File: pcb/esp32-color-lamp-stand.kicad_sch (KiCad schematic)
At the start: 56 parts, among them J1 USB_C_Receptacle, U1 MIC5219-3.3YM5, U2 ESP32-WROOM-32, U3 CH340G, U4 74HCT245

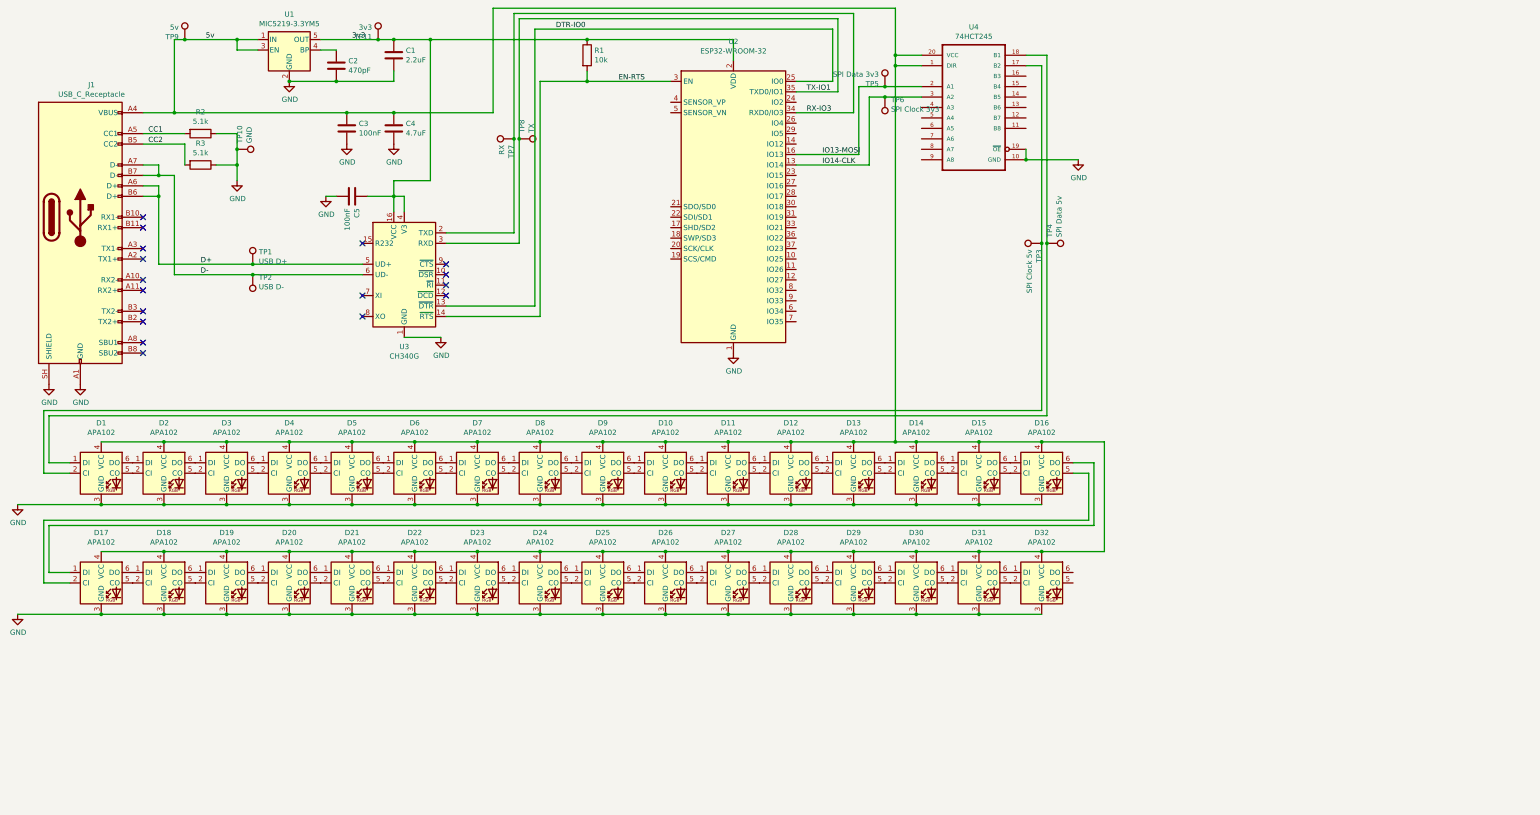
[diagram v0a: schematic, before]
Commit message: Complete ESP32-S3 PCB redesign and routing
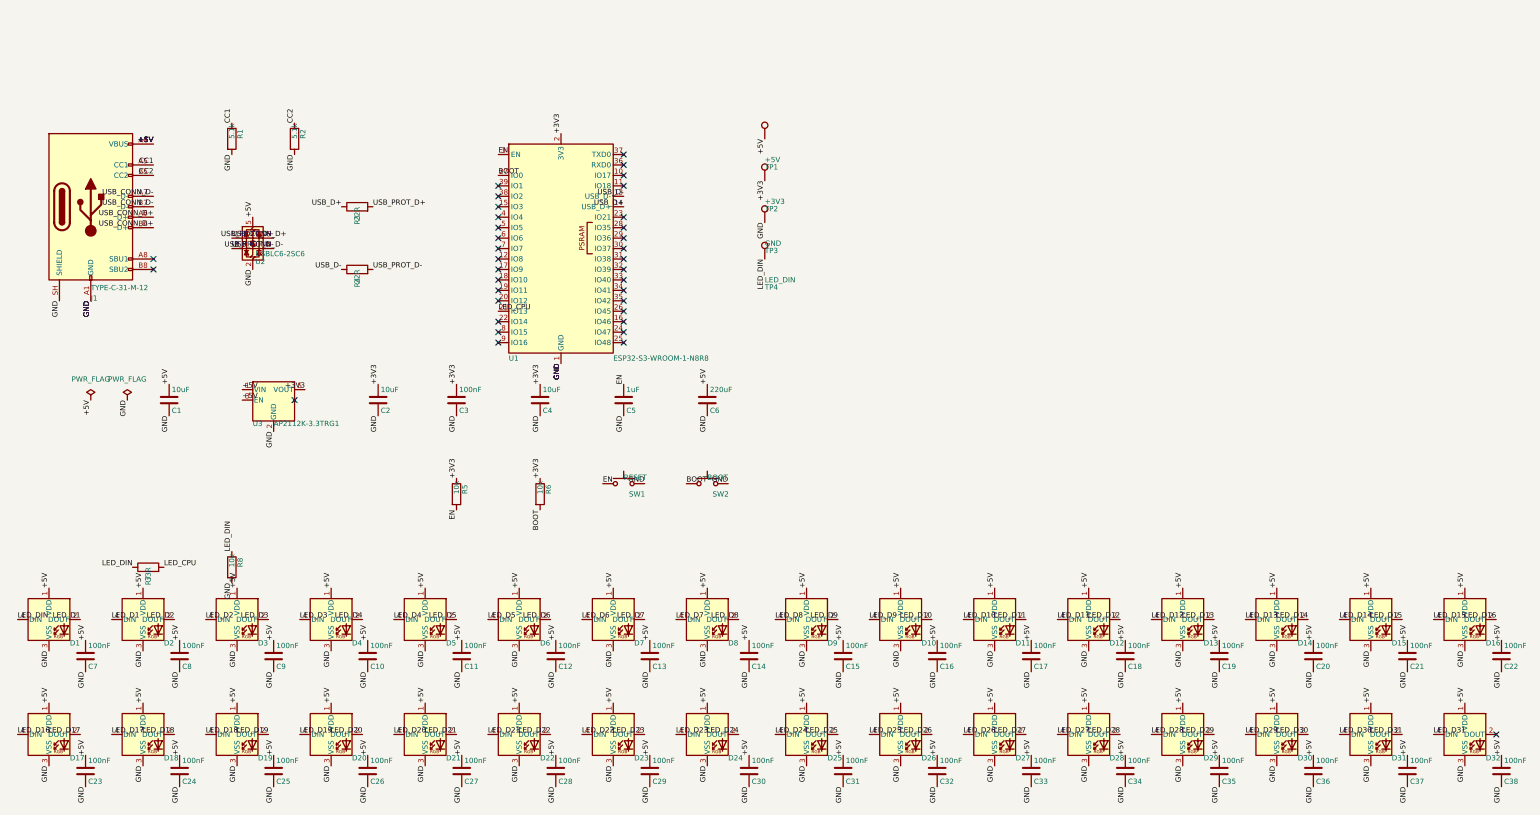
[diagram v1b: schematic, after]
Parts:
- removed D1, D10, D11, D12, D13, D14, D15, D16, D17, D18, D19, D2, D20, D21, D22, D23, D24, D25, D26, D27, D28, D29, D3, D30, D31, D32, D4, D5, D6, D7, D8, D9: APA102, LED_SMD:LED_RGB_5050-6, symbol LED:APA102
- removed J1: USB_C_Receptacle, Connector_USB:USB_C_Receptacle_Amphenol_12401610E4-2A_CircularHoles, symbol Connector:USB_C_Receptacle
- removed TP10: GND, TestPoint:TestPoint_Pad_D1.0mm, symbol Connector:TestPoint
- removed TP11: 3v3, TestPoint:TestPoint_Pad_D1.0mm, symbol Connector:TestPoint
- removed TP5: SPI Data 3v3, TestPoint:TestPoint_Pad_D1.0mm, symbol Connector:TestPoint
- removed TP6: SPI Clock 3v3, TestPoint:TestPoint_Pad_D1.0mm, symbol Connector:TestPoint
- removed TP7: RX, TestPoint:TestPoint_Pad_D1.0mm, symbol Connector:TestPoint
- removed TP8: TX, TestPoint:TestPoint_Pad_D1.0mm, symbol Connector:TestPoint
- removed TP9: 5v, TestPoint:TestPoint_Pad_D1.0mm, symbol Connector:TestPoint
- removed U1: MIC5219-3.3YM5, Package_TO_SOT_SMD:SOT-23-5, symbol Regulator_Linear:MIC5219-3.3YM5
- removed U2: ESP32-WROOM-32, RF_Module:ESP32-WROOM-32, symbol RF_Module:ESP32-WROOM-32
- removed U3: CH340G, Package_SO:SOIC-16_3.9x9.9mm_P1.27mm, symbol Interface_USB:CH340G
- removed U4: 74HCT245, 74HCT245:SSOP20, symbol 74HCT245:74HCT245
- added C10, C11, C12, C13, C14, C15, C16, C17, C18, C19, C20, C21, C22, C23, C24, C25, C26, C27, C28, C29, C30, C31, C32, C33, C34, C35, C36, C37, C38, C7, C8, C9: 100nF, Capacitor_SMD:C_0603_1608Metric, symbol Device:C
- added C6: 220uF, Capacitor_SMD:C_Elec_5x5.8, symbol Device:C
- added D1, D10, D11, D12, D13, D14, D15, D16, D17, D18, D19, D2, D20, D21, D22, D23, D24, D25, D26, D27, D28, D29, D3, D30, D31, D32, D4, D5, D6, D7, D8, D9: XL-5050RGBC-2812B-S, LED_SMD:LED_WS2812B_PLCC4_5.0x5.0mm_P3.2mm, symbol LED:WS2812B
- added J1: TYPE-C-31-M-12, Connector_USB:USB_C_Receptacle_HRO_TYPE-C-31-M-12, symbol Connector:USB_C_Receptacle_USB2.0_16P
- added R4: 22R, Resistor_SMD:R_0603_1608Metric, symbol Device:R
- added R5, R6, R8: 10k, Resistor_SMD:R_0603_1608Metric, symbol Device:R
- added R7: 33R, Resistor_SMD:R_0603_1608Metric, symbol Device:R
- added SW1: RESET, Button_Switch_SMD:SW_Push_1P1T_XKB_TS-1187A, symbol Switch:SW_Push
- added SW2: BOOT, Button_Switch_SMD:SW_Push_1P1T_XKB_TS-1187A, symbol Switch:SW_Push
- added U1: ESP32-S3-WROOM-1-N8R8, RF_Module:ESP32-S3-WROOM-1, symbol RF_Module:ESP32-S3-WROOM-1
- added U2: USBLC6-2SC6, Package_TO_SOT_SMD:SOT-23-6, symbol Power_Protection:USBLC6-2SC6
- added U3: AP2112K-3.3TRG1, Package_TO_SOT_SMD:SOT-23-5, symbol Regulator_Linear:AP2112K-3.3
- C1: value 2.2uF -> 10uF; LCSC (none) -> C15850; Manufacturer (none) -> Samsung Electro-Mechanics; Manufacturer Part Number (none) -> 10uF
- C2: value 470pF -> 10uF; LCSC (none) -> C15850; Manufacturer (none) -> Samsung Electro-Mechanics; Manufacturer Part Number (none) -> 10uF
- C3: footprint Capacitor_SMD:C_0805_2012Metric -> Capacitor_SMD:C_0603_1608Metric; LCSC (none) -> C14663; Manufacturer (none) -> Samsung Electro-Mechanics; Manufacturer Part Number (none) -> 100nF
- C4: value 4.7uF -> 10uF; LCSC (none) -> C15850; Manufacturer (none) -> Samsung Electro-Mechanics; Manufacturer Part Number (none) -> 10uF
- C5: value 100nF -> 1uF; footprint Capacitor_SMD:C_0805_2012Metric -> Capacitor_SMD:C_0603_1608Metric; LCSC (none) -> C15849; Manufacturer (none) -> Samsung Electro-Mechanics; Manufacturer Part Number (none) -> 1uF
- R1: value 10k -> 5.1k; footprint Resistor_SMD:R_0805_2012Metric -> Resistor_SMD:R_0603_1608Metric; LCSC (none) -> C23186; Manufacturer (none) -> UNI-ROYAL; Manufacturer Part Number (none) -> 5.1k
- R2: footprint Resistor_SMD:R_0805_2012Metric -> Resistor_SMD:R_0603_1608Metric; LCSC (none) -> C23186; Manufacturer (none) -> UNI-ROYAL; Manufacturer Part Number (none) -> 5.1k
- R3: value 5.1k -> 22R; footprint Resistor_SMD:R_0805_2012Metric -> Resistor_SMD:R_0603_1608Metric; LCSC (none) -> C23345; Manufacturer (none) -> UNI-ROYAL; Manufacturer Part Number (none) -> 22R
- TP1: value USB D+ -> +5V; footprint TestPoint:TestPoint_Pad_D1.0mm -> TestPoint:TestPoint_Pad_D1.5mm; LCSC (none) -> DNP; Manufacturer (none) -> DNP; Manufacturer Part Number (none) -> DNP; now left out of the parts list
- TP2: value USB D- -> +3V3; footprint TestPoint:TestPoint_Pad_D1.0mm -> TestPoint:TestPoint_Pad_D1.5mm; LCSC (none) -> DNP; Manufacturer (none) -> DNP; Manufacturer Part Number (none) -> DNP; now left out of the parts list
- TP3: value SPI Clock 5v -> GND; footprint TestPoint:TestPoint_Pad_D1.0mm -> TestPoint:TestPoint_Pad_D1.5mm; LCSC (none) -> DNP; Manufacturer (none) -> DNP; Manufacturer Part Number (none) -> DNP; now left out of the parts list
- TP4: value SPI Data 5v -> LED_DIN; footprint TestPoint:TestPoint_Pad_D1.0mm -> TestPoint:TestPoint_Pad_D1.5mm; LCSC (none) -> DNP; Manufacturer (none) -> DNP; Manufacturer Part Number (none) -> DNP; now left out of the parts list
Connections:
- net 5v is gone; now on net +3V3: C3.1, C4.1
- net D- is gone; now on net +3V3: TP2.1
- net EN-RTS is gone; now on net GND: R1.2
- net CC1: now also R1.1, J1.A5 (CC1); no longer R2.2
- net CC2: now also R2.1, J1.B5 (CC2); no longer R3.2
- net GND: now also R2.2, TP3.1, C10.2, C11.2, C12.2, C13.2, C14.2, C15.2, C16.2, C17.2, C18.2, C19.2, C20.2, C21.2, C22.2, C23.2, C24.2, C25.2, C26.2, C27.2, C28.2, C29.2, C30.2, C31.2, C32.2, C33.2, C34.2, C35.2, C36.2, C37.2, C38.2, C6.2, C7.2, C8.2, C9.2, D1.3 (VSS), D10.3 (VSS), D11.3 (VSS), D12.3 (VSS), D13.3 (VSS), D14.3 (VSS), D15.3 (VSS), D16.3 (VSS), D17.3 (VSS), D18.3 (VSS), D19.3 (VSS), D2.3 (VSS), D20.3 (VSS), D21.3 (VSS), D22.3 (VSS), D23.3 (VSS), D24.3 (VSS), D25.3 (VSS), D26.3 (VSS), D27.3 (VSS), D28.3 (VSS), D29.3 (VSS), D3.3 (VSS), D30.3 (VSS), D31.3 (VSS), D32.3 (VSS), D4.3 (VSS), D5.3 (VSS), D6.3 (VSS), D7.3 (VSS), D8.3 (VSS), D9.3 (VSS), J1.A1 (GND), J1.A12 (GND), J1.B1 (GND), J1.B12 (GND), J1.SH (SHIELD), R8.2, SW1.2, SW2.2, U1.1 (GND), U1.40 (GND), U1.41 (GND), U2.2 (GND), U3.2 (GND); no longer R2.1, R3.1
- net +3V3: now reaches C2.1
- net +3V3: now also R5.1, R6.1, U1.2 (3V3), U3.5 (VOUT)
- net LED_DIN: now reaches TP4.1
- net LED_DIN: now also D1.4 (DIN), R7.1, R8.1
- removed net 3v3: C1.1, C5.1, R1.1
- net D+ renamed +5V
- net +5V: now also C1.1, C10.1, C11.1, C12.1, C13.1, C14.1, C15.1, C16.1, C17.1, C18.1, C19.1, C20.1, C21.1, C22.1, C23.1, C24.1, C25.1, C26.1, C27.1, C28.1, C29.1, C30.1, C31.1, C32.1, C33.1, C34.1, C35.1, C36.1, C37.1, C38.1, C6.1, C7.1, C8.1, C9.1, D1.1 (VDD), D10.1 (VDD), D11.1 (VDD), D12.1 (VDD), D13.1 (VDD), D14.1 (VDD), D15.1 (VDD), D16.1 (VDD), D17.1 (VDD), D18.1 (VDD), D19.1 (VDD), D2.1 (VDD), D20.1 (VDD), D21.1 (VDD), D22.1 (VDD), D23.1 (VDD), D24.1 (VDD), D25.1 (VDD), D26.1 (VDD), D27.1 (VDD), D28.1 (VDD), D29.1 (VDD), D3.1 (VDD), D30.1 (VDD), D31.1 (VDD), D32.1 (VDD), D4.1 (VDD), D5.1 (VDD), D6.1 (VDD), D7.1 (VDD), D8.1 (VDD), D9.1 (VDD), J1.A4 (VBUS), J1.A9 (VBUS), J1.B4 (VBUS), J1.B9 (VBUS), U2.5 (VBUS), U3.1 (VIN), U3.3 (EN)
- new net BOOT: R6.2, SW2.1, U1.27 (IO0)
- new net EN: C5.1, R5.2, SW1.1, U1.3 (EN)
- new net LED_CPU: R7.2, U1.21 (IO13)
- new net LED_D1: D1.2 (DOUT), D2.4 (DIN)
- new net LED_D10: D10.2 (DOUT), D11.4 (DIN)
- new net LED_D11: D11.2 (DOUT), D12.4 (DIN)
- new net LED_D12: D12.2 (DOUT), D13.4 (DIN)
- new net LED_D13: D13.2 (DOUT), D14.4 (DIN)
- new net LED_D14: D14.2 (DOUT), D15.4 (DIN)
- new net LED_D15: D15.2 (DOUT), D16.4 (DIN)
- new net LED_D16: D16.2 (DOUT), D17.4 (DIN)
- new net LED_D17: D17.2 (DOUT), D18.4 (DIN)
- new net LED_D18: D18.2 (DOUT), D19.4 (DIN)
- new net LED_D19: D19.2 (DOUT), D20.4 (DIN)
- new net LED_D2: D2.2 (DOUT), D3.4 (DIN)
- new net LED_D20: D20.2 (DOUT), D21.4 (DIN)
- new net LED_D21: D21.2 (DOUT), D22.4 (DIN)
- new net LED_D22: D22.2 (DOUT), D23.4 (DIN)
- new net LED_D23: D23.2 (DOUT), D24.4 (DIN)
- new net LED_D24: D24.2 (DOUT), D25.4 (DIN)
- new net LED_D25: D25.2 (DOUT), D26.4 (DIN)
- new net LED_D26: D26.2 (DOUT), D27.4 (DIN)
- new net LED_D27: D27.2 (DOUT), D28.4 (DIN)
- new net LED_D28: D28.2 (DOUT), D29.4 (DIN)
- new net LED_D29: D29.2 (DOUT), D30.4 (DIN)
- new net LED_D3: D3.2 (DOUT), D4.4 (DIN)
- new net LED_D30: D30.2 (DOUT), D31.4 (DIN)
- new net LED_D31: D31.2 (DOUT), D32.4 (DIN)
- new net LED_D4: D4.2 (DOUT), D5.4 (DIN)
- new net LED_D5: D5.2 (DOUT), D6.4 (DIN)
- new net LED_D6: D6.2 (DOUT), D7.4 (DIN)
- new net LED_D7: D7.2 (DOUT), D8.4 (DIN)
- new net LED_D8: D8.2 (DOUT), D9.4 (DIN)
- new net LED_D9: D10.4 (DIN), D9.2 (DOUT)
- new net USB_CONN_D+: J1.A6 (D+), J1.B6 (D+), U2.1 (I/O1)
- new net USB_CONN_D-: J1.A7 (D-), J1.B7 (D-), U2.3 (I/O2)
- new net USB_D+: R3.1, U1.14 (USB_D+)
- new net USB_D-: R4.1, U1.13 (USB_D-)
- new net USB_PROT_D+: R3.2, U2.6 (I/O1)
- new net USB_PROT_D-: R4.2, U2.4 (I/O2)
- no-connect marks 17 -> 36
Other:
- title: (none) -> esp32-color-lamp-stand

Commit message: Finalize ESP32-S3 PCB and manufacturing workflow
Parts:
- removed C6: 220uF, Capacitor_SMD:C_Elec_5x5.8, symbol Device:C
- added C39, C42, C43: 100nF, Capacitor_SMD:C_0603_1608Metric, symbol Device:C
- added C40: 10nF, Capacitor_SMD:C_0603_1608Metric, symbol Device:C
- added C41: 1uF, Capacitor_SMD:C_0603_1608Metric, symbol Device:C
- added C6: 220uF, Capacitor_SMD:C_Elec_6.3x5.8, symbol Device:C_Polarized
- added R10, R11, R12, R9: 100k, Resistor_SMD:R_0603_1608Metric, symbol Device:R
- added TP5: LED_5V, TestPoint:TestPoint_Pad_D1.0mm, symbol Connector:TestPoint
- added U4: 74AHCT1G125W5-7, Package_TO_SOT_SMD:SOT-23-5, symbol 74xGxx:74AHCT1G125
- added U5: TPS22975DSGR, Package_SON:Texas_DSG0008A_WSON-8-1EP_2x2mm_P0.5mm_EP0.9x1.6mm, symbol esp32-color-lamp-stand-symbols:TPS22975DSGR
- C1: value 10uF -> 4.7uF; LCSC C15850 -> C1779; Manufacturer Part Number 10uF -> 4.7uF
- R7: value 33R -> 470R; LCSC C23140 -> C23179; Manufacturer Part Number 33R -> 470R
- TP1, TP2, TP3, TP4: footprint TestPoint:TestPoint_Pad_D1.5mm -> TestPoint:TestPoint_Pad_D1.0mm
- U3: LCSC C51118 -> C23380830
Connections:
- net +3V3: now also U5.3 (ON)
- net +5V: now also C41.1, U5.4 (VIN), U5.5 (VBIAS), U5.6 (VIN); no longer C10.1, C11.1, C12.1, C13.1, C14.1, C15.1, C16.1, C17.1, C18.1, C19.1, C20.1, C21.1, C22.1, C23.1, C24.1, C25.1, C26.1, C27.1, C28.1, C29.1, C30.1, C31.1, C32.1, C33.1, C34.1, C35.1, C36.1, C37.1, C38.1, C7.1, C8.1, C9.1, D1.1 (VDD), D10.1 (VDD), D11.1 (VDD), D12.1 (VDD), D13.1 (VDD), D14.1 (VDD), D15.1 (VDD), D16.1 (VDD), D17.1 (VDD), D18.1 (VDD), D19.1 (VDD), D2.1 (VDD), D20.1 (VDD), D21.1 (VDD), D22.1 (VDD), D23.1 (VDD), D24.1 (VDD), D25.1 (VDD), D26.1 (VDD), D27.1 (VDD), D28.1 (VDD), D29.1 (VDD), D3.1 (VDD), D30.1 (VDD), D31.1 (VDD), D32.1 (VDD), D4.1 (VDD), D5.1 (VDD), D6.1 (VDD), D7.1 (VDD), D8.1 (VDD), D9.1 (VDD)
- net BOOT: now also SW2.2; no longer SW2.1
- net CC1: now also R9.1
- net CC2: now also R10.1
- net EN: now also SW1.2; no longer SW1.1
- net GND: now also SW1.1, SW2.1, C39.2, C40.2, C41.2, C42.2, C43.2, C6.2, R11.2, R12.2, U4.1, U4.3 (GND), U5.2 (GND), U5.9 (EP); no longer SW1.2, SW2.2
- net LED_CPU: now also R8.1, U4.2; no longer R7.2
- net LED_DIN: no longer R8.1
- net CC1_ADC: now reaches U1.4 (IO4)
- net CC1_ADC: now also C42.1, R11.1, R9.2
- net CC2_ADC: now reaches U1.5 (IO5)
- net CC2_ADC: now also C43.1, R10.2, R12.1
- net LED_D1: no longer names the net of D1.2 (DOUT), D2.4 (DIN)
- net LED_D10: no longer names the net of D10.2 (DOUT), D11.4 (DIN)
- net LED_D11: no longer names the net of D11.2 (DOUT), D12.4 (DIN)
- net LED_D12: no longer names the net of D12.2 (DOUT), D13.4 (DIN)
- net LED_D13: no longer names the net of D13.2 (DOUT), D14.4 (DIN)
- net LED_D14: no longer names the net of D14.2 (DOUT), D15.4 (DIN)
- net LED_D15: no longer names the net of D15.2 (DOUT), D16.4 (DIN)
- net LED_D17: no longer names the net of D17.2 (DOUT), D18.4 (DIN)
- net LED_D18: no longer names the net of D18.2 (DOUT), D19.4 (DIN)
- net LED_D19: no longer names the net of D19.2 (DOUT), D20.4 (DIN)
- net LED_D2: no longer names the net of D2.2 (DOUT), D3.4 (DIN)
- net LED_D20: no longer names the net of D20.2 (DOUT), D21.4 (DIN)
- net LED_D21: no longer names the net of D21.2 (DOUT), D22.4 (DIN)
- net LED_D22: no longer names the net of D22.2 (DOUT), D23.4 (DIN)
- net LED_D23: no longer names the net of D23.2 (DOUT), D24.4 (DIN)
- net LED_D24: no longer names the net of D24.2 (DOUT), D25.4 (DIN)
- net LED_D25: no longer names the net of D25.2 (DOUT), D26.4 (DIN)
- net LED_D26: no longer names the net of D26.2 (DOUT), D27.4 (DIN)
- net LED_D27: no longer names the net of D27.2 (DOUT), D28.4 (DIN)
- net LED_D28: no longer names the net of D28.2 (DOUT), D29.4 (DIN)
- net LED_D29: no longer names the net of D29.2 (DOUT), D30.4 (DIN)
- net LED_D3: no longer names the net of D3.2 (DOUT), D4.4 (DIN)
- net LED_D30: no longer names the net of D30.2 (DOUT), D31.4 (DIN)
- net LED_D31: no longer names the net of D31.2 (DOUT), D32.4 (DIN)
- net LED_D4: no longer names the net of D4.2 (DOUT), D5.4 (DIN)
- net LED_D5: no longer names the net of D5.2 (DOUT), D6.4 (DIN)
- net LED_D6: no longer names the net of D6.2 (DOUT), D7.4 (DIN)
- net LED_D7: no longer names the net of D7.2 (DOUT), D8.4 (DIN)
- net LED_D8: no longer names the net of D8.2 (DOUT), D9.4 (DIN)
- net LED_D9: no longer names the net of D10.4 (DIN), D9.2 (DOUT)
- new net LED_5V: C10.1, C11.1, C12.1, C13.1, C14.1, C15.1, C16.1, C17.1, C18.1, C19.1, C20.1, C21.1, C22.1, C23.1, C24.1, C25.1, C26.1, C27.1, C28.1, C29.1, C30.1, C31.1, C32.1, C33.1, C34.1, C35.1, C36.1, C37.1, C38.1, C39.1, C6.1, C7.1, C8.1, C9.1, D1.1 (VDD), D10.1 (VDD), D11.1 (VDD), D12.1 (VDD), D13.1 (VDD), D14.1 (VDD), D15.1 (VDD), D16.1 (VDD), D17.1 (VDD), D18.1 (VDD), D19.1 (VDD), D2.1 (VDD), D20.1 (VDD), D21.1 (VDD), D22.1 (VDD), D23.1 (VDD), D24.1 (VDD), D25.1 (VDD), D26.1 (VDD), D27.1 (VDD), D28.1 (VDD), D29.1 (VDD), D3.1 (VDD), D30.1 (VDD), D31.1 (VDD), D32.1 (VDD), D4.1 (VDD), D5.1 (VDD), D6.1 (VDD), D7.1 (VDD), D8.1 (VDD), D9.1 (VDD), TP5.1, U4.5 (VCC), U5.7 (VOUT), U5.8 (VOUT)
- new net LED_BUFFERED: R7.2, U4.4
- new net TPS_CT: C40.1, U5.1 (CT)
- no-connect marks 36 -> 34
